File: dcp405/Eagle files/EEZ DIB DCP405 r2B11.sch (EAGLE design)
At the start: 320 parts, among them IC1 LTC3864EMSE#PBF, IC10 MC33272ADR2G, IC11 LTC2050HVCS8#PBF, IC12 74AUP1G74DC.125, IC13 MCP23S17-E/SS, IC14 REF5025AIDR, IC15 TC77-5.0MCTTR, IC16 DAC8552IDGKR, IC17 SN74LVC1G3157DCKR, IC18 ADS1120IPWR, IC19 LM293D, IC2 TPS54060DGQ, IC20 MAX9141ESA, IC3 SI8641BB-B-IS1, IC4 SN74LVC1G139DCUR, IC5 MC78L05, IC6 MC79L05, IC7 SI8641BB-B-IS1, IC8 M24C32-WMN6P, IC9 TL072D, J1 4907, J2 FCR7350R, J3 FCR7350B, K1 G6K-2F-5DC, Q1 SUD19P06-60, Q10 PSMN0R9-25YLC, Q11 PSMN0R9-25YLC, Q12 BSS84P, Q13 BTA26-600, Q14 FMMT493TA, Q15 2N7002, Q16 2N7002, Q17 2N7002, Q18 PSMN013-60YL, Q19 MMBT5551, Q2 MMBT5401, Q20 MMBT5401, Q21 MMBT5551, Q22 MMBT5551, Q23 2N7002, Q3 D45H11FP, Q4 D45H11FP, Q5 FQPF11P06 or FQPF27P06, Q6 BCP56-16.115, Q7 MMBT5401, Q8 NZT605, Q9 BSS205NH6327XTSA1, X1 39-30-1020, X2 77317-104-20LF, X3 691322110005, X4 DS1024-2*10R0

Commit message: DCP405 r2B11
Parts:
- added IC21: SN74LVC1G3157DCKR, EEZ_Lib1:SN74LVC1G3157-DCK
- added Q27: 2N7002, EEZ_Lib1:2N7002
- added R115: 220R, rcl:R-EU_R0805
- added R116: 470R, rcl:R-EU_R0805
- added R118: 22K, rcl:R-EU_R0805
- C55: value 1n -> 4n7
- C62: value N.C. -> 100n; device rcl:C-EUC0805 -> rcl:C-EUC0603
- IC10: value MC33272ADR2G -> TL072D
- R44, R53: value 16K -> 10K
- R62: value 10K -> 47K
- R63: value 220R -> 8K2
- R66: value 750R -> 3K3
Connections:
- new net N$54: IC11A.OUT, R115.2
- new net N$57: IC21.NO, R116.1
- new net N$58: Q27.D, R118.1
- net CC_ACTIVE: now also Q27.G
- net CURR_5A: now also IC21.CTRL
- net GND: now also C62.2, IC21.GND, Q27.S
- net ISENSE-: no longer C62.1
- net I_MON: now also D17.C, IC21.COM, R115.1; no longer C62.2, IC11A.OUT
- net N$81: no longer D17.C
- net N$89: now also R116.2
- net U_SET_OVP: now also R118.2
- net V+: now also C62.1, IC21.VDD
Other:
- note removed: "Parts with red marked values are installed on DCP405 only"
- note removed: "Parts with red marked values are installed on DCP405 only Solder JP2 (0R 0805) on DCP405B"
- note removed: "Parts with red marked values are installed on DCP405 only Solder JP3, JP4 (0R 0805) and use wire jumper instead of F1 and F2 on DCP405B"
- moved on the sheet: C41, C48, C55, C60, C61, C62, D14, D17, IC10A, IC11A, Q10, Q11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

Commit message: DCP405 BOM update
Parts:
- C45: value 1u -> N.C.
- R54: value 4K7 -> 220R
- R55: value N.C. -> 100K
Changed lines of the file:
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@@
 <setting verticaltext="up"/>
 </settings>
-<grid distance="0.1" unitdist="inch" unit="inch" style="lines" multiple="1" display="no" altdistance="0.01" altunitdist="inch" altunit="inch"/>
+<grid distance="0.025" unitdist="inch" unit="inch" style="lines" multiple="4" display="no" altdistance="0.01" altunitdist="inch" altunit="inch"/>
 <layers>
 <layer number="1" name="Top" color="4" fill="1" visible="no" active="no"/>
@@
 <part name="C81" library="rcl" deviceset="C-EU" device="C0603" value="100n"/>
 <part name="C79" library="rcl" deviceset="C-EU" device="C0603" value="100n"/>
-<part name="R55" library="rcl" deviceset="R-EU_" device="R0805" value="N.C."/>
+<part name="R55" library="rcl" deviceset="R-EU_" device="R0805" value="100K"/>
 <part name="P+29" library="supply1" deviceset="+5V" device=""/>
 <part name="R72" library="rcl" deviceset="R-EU_" device="R0805" value="100K"/>
@@
 <part name="R101" library="rcl" deviceset="R-EU_" device="R0805" value="1K"/>
 <part name="R43" library="rcl" deviceset="R-EU_" device="R0805" value="1K"/>
-<part name="R54" library="rcl" deviceset="R-EU_" device="R0805" value="4K7"/>
+<part name="R54" library="rcl" deviceset="R-EU_" device="R0805" value="220R"/>
 <part name="D11" library="EEZ_Lib1" deviceset="DIODE" device="SOD323R" value="BAS316"/>
 <part name="R28" library="rcl" deviceset="R-EU_" device="R0805" value="N.C."/>
@@
 <part name="SUPPLY27" library="supply2" deviceset="-9V" device=""/>
 <part name="SUPPLY44" library="supply2" deviceset="-9V" device=""/>
-<part name="C45" library="rcl" deviceset="C-EU" device="C0805" value="1u"/>
+<part name="C45" library="rcl" deviceset="C-EU" device="C0805" value="N.C."/>
 <part name="SUPPLY6" library="supply2" deviceset="-9V" device=""/>
 <part name="R87" library="rcl" deviceset="R-EU_" device="R0805" value="10K"/>
@@
 <rectangle x1="203.835" y1="91.44" x2="210.82" y2="96.52" layer="97"/>
 <rectangle x1="116.205" y1="130.175" x2="122.555" y2="136.525" layer="97"/>
+<rectangle x1="53.975" y1="76.2" x2="60.96" y2="81.28" layer="97"/>
 </plain>
 <instances>

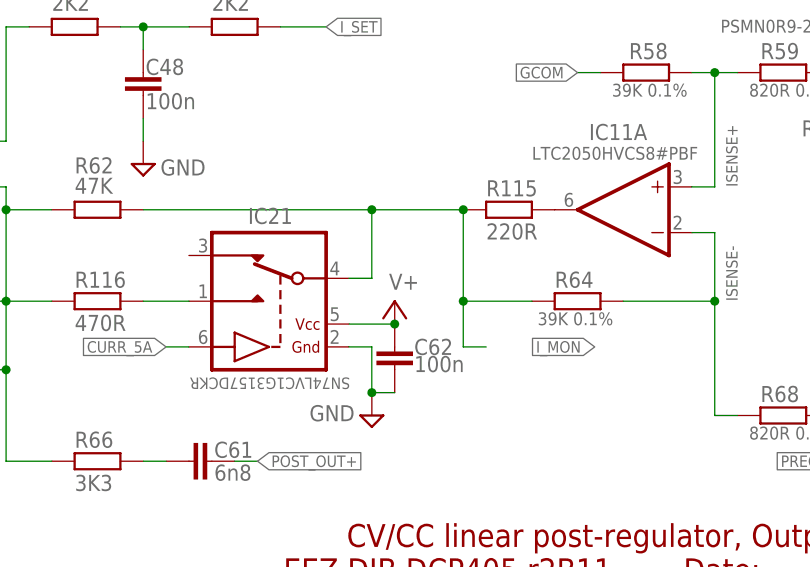
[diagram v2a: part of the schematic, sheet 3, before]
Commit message: DCP405 OVP adjustment
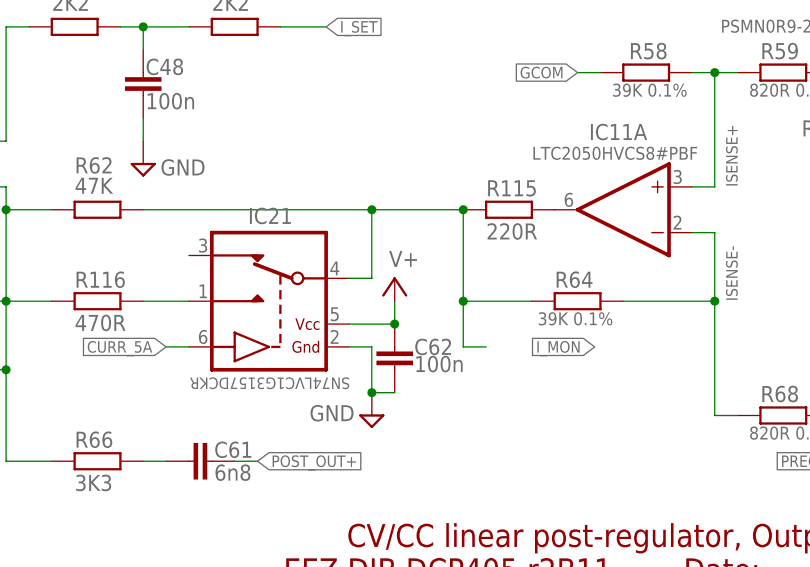
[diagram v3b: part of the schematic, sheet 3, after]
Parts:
- C64: value 1n -> 4n7
- C86: value 1n -> N.C.
- C87: value 33n -> 4n7
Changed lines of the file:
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@@
 <setting verticaltext="up"/>
 </settings>
-<grid distance="0.025" unitdist="inch" unit="inch" style="lines" multiple="4" display="no" altdistance="0.01" altunitdist="inch" altunit="inch"/>
+<grid distance="0.1" unitdist="inch" unit="inch" style="lines" multiple="1" display="no" altdistance="0.01" altunitdist="inch" altunit="inch"/>
 <layers>
 <layer number="1" name="Top" color="4" fill="1" visible="no" active="no"/>
@@
 <part name="R83" library="rcl" deviceset="R-EU_" device="R0805" value="330R"/>
 <part name="R89" library="rcl" deviceset="R-EU_" device="R0805" value="10K"/>
-<part name="C86" library="rcl" deviceset="C-EU" device="C0805" value="1n"/>
+<part name="C86" library="rcl" deviceset="C-EU" device="C0805" value="N.C."/>
 <part name="P+11" library="supply2" deviceset="V+" device=""/>
 <part name="SUPPLY12" library="supply2" deviceset="GND" device=""/>
@@
 <part name="F1" library="EEZ_Lib1" deviceset="ZH32" device="" value="ZH32"/>
 <part name="F2" library="EEZ_Lib1" deviceset="ZH32" device="" value="ZH32"/>
-<part name="C87" library="rcl" deviceset="C-EU" device="C0805" value="33n"/>
+<part name="C87" library="rcl" deviceset="C-EU" device="C0805" value="4n7"/>
 <part name="+3V5" library="supply1" deviceset="+3V3" device=""/>
 <part name="GND2" library="supply1" deviceset="GNDIO" device=""/>
@@
 <part name="C40" library="rcl" deviceset="C-EU" device="C0805" value="N.C."/>
 <part name="JP1" library="EEZ_Lib1" deviceset="JP2-NOCUT" device=""/>
-<part name="C64" library="rcl" deviceset="C-EU" device="C0805" value="1n"/>
+<part name="C64" library="rcl" deviceset="C-EU" device="C0805" value="4n7"/>
 <part name="FM3" library="EEZ_Lib1" deviceset="FIDUCIAL" device="_2"/>
 <part name="D8" library="EEZ_Lib1" deviceset="SCHOTTKY" device="SOD123" value="N.C."/>
@@
 <attribute name="VALUE" x="162.179" y="25.146" size="1.778" layer="96"/>
 </instance>
-<instance part="P+14" gate="1" x="160.02" y="33.02" smashed="yes">
-<attribute name="VALUE" x="159.385" y="34.29" size="1.778" layer="96"/>
+<instance part="P+14" gate="1" x="160.02" y="35.56" smashed="yes">
+<attribute name="VALUE" x="159.385" y="36.83" size="1.778" layer="96"/>
 </instance>
 </instances>
@@
 <pinref part="IC21" gate="G$1" pin="VDD"/>
 <pinref part="C62" gate="G$1" pin="1"/>
-<wire x1="154.94" y1="30.48" x2="160.02" y2="30.48" width="0.1524" layer="91"/>
 <pinref part="P+14" gate="1" pin="V+"/>
+<wire x1="160.02" y1="33.02" x2="160.02" y2="30.48" width="0.1524" layer="91"/>
+<wire x1="154.94" y1="30.48" x2="160.02" y2="30.48" width="0.1524" layer="91"/>
 <junction x="160.02" y="30.48"/>
 </segment>
@@
 <rectangle x1="158.75" y1="135.255" x2="165.1" y2="142.875" layer="97"/>
 <wire x1="259.08" y1="50.8" x2="119.38" y2="50.8" width="0.1524" layer="97" style="shortdash"/>
+<rectangle x1="147.32" y1="129.54" x2="152.4" y2="137.16" layer="97"/>
 </plain>
 <instances>

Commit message: DCP405 fuse rating changed
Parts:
- J2, J3: device EEZ_Lib1:BINDING_POSTCLIFF -> EEZ_connectors:BINDING_POSTCLIFF
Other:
- note added: "5 A quick blow fuse e.g. 179020.5"
- note removed: "Use 6.3A high Breaking capacity fuse e.g. ESKA 522.725"
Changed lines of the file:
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@@
 <layer number="111" name="111" color="7" fill="1" visible="no" active="no"/>
 <layer number="112" name="tSilk" color="7" fill="1" visible="no" active="no"/>
+<layer number="113" name="bTPoint" color="7" fill="1" visible="no" active="no"/>
 <layer number="114" name="EEZ" color="12" fill="1" visible="yes" active="yes"/>
 <layer number="116" name="Patch_BOT" color="7" fill="1" visible="no" active="no"/>
 <layer number="118" name="Rect_Pads" color="7" fill="1" visible="no" active="no"/>
+<layer number="120" name="lotbs" color="7" fill="1" visible="no" active="no"/>
 <layer number="121" name="_tsilk" color="7" fill="1" visible="no" active="no"/>
 <layer number="122" name="_bsilk" color="7" fill="1" visible="no" active="no"/>
@@
 <layer number="132" name="bAdjust" color="7" fill="1" visible="no" active="no"/>
 <layer number="144" name="Drill_legend" color="7" fill="1" visible="no" active="no"/>
+<layer number="148" name="Document_mirrored" color="7" fill="1" visible="no" active="no"/>
 <layer number="150" name="Notes" color="7" fill="1" visible="no" active="no"/>
 <layer number="151" name="HeatSink" color="14" fill="1" visible="no" active="no"/>
@@
 <layer number="154" name="FabDoc2" color="2" fill="1" visible="no" active="no"/>
 <layer number="155" name="FabDoc3" color="7" fill="15" visible="no" active="no"/>
+<layer number="156" name="gesam-Maß" color="1" fill="7" visible="no" active="no"/>
+<layer number="157" name="FaceMchng" color="3" fill="1" visible="no" active="no"/>
+<layer number="158" name="FaceMMeas" color="3" fill="1" visible="no" active="no"/>
+<layer number="159" name="Geh-Bear2" color="1" fill="7" visible="no" active="no"/>
+<layer number="160" name="Topologie" color="9" fill="1" visible="no" active="no"/>
+<layer number="161" name="tomplace2" color="7" fill="1" visible="no" active="no"/>
 <layer number="199" name="Contour" color="7" fill="1" visible="no" active="no"/>
 <layer number="200" name="200bmp" color="1" fill="10" visible="no" active="no"/>
@@
 <layer number="250" name="Descript" color="7" fill="1" visible="no" active="no"/>
 <layer number="251" name="SMDround" color="7" fill="1" visible="no" active="no"/>
+<layer number="252" name="BR-BS" color="7" fill="1" visible="no" active="no"/>
+<layer number="253" name="BR-LS" color="7" fill="1" visible="no" active="no"/>
 <layer number="254" name="OrgLBR" color="13" fill="1" visible="no" active="no"/>
+<layer number="255" name="ZchnBlatt" color="7" fill="1" visible="no" active="no"/>
 </layers>
 <schematic xreflabel="%F%N/%S.%C%R" xrefpart="/%S.%C%R">
@@
 <part name="SUPPLY46" library="supply2" deviceset="GND" device=""/>
 <part name="SUPPLY47" library="supply2" deviceset="GND" device=""/>
-<part name="J3" library="EEZ_Lib1" deviceset="BINDING_POST" device="CLIFF" value="FCR7350B"/>
-<part name="J2" library="EEZ_Lib1" deviceset="BINDING_POST" device="CLIFF" value="FCR7350R"/>
+<part name="J3" library="EEZ_connectors" deviceset="BINDING_POST" device="CLIFF" value="FCR7350B"/>
+<part name="J2" library="EEZ_connectors" deviceset="BINDING_POST" device="CLIFF" value="FCR7350R"/>
 <part name="FRAME6" library="frames" deviceset="DINA4_L" device=""/>
 <part name="R88" library="rcl" deviceset="R-EU_" device="R0805" value="4K7"/>
@@
 <text x="93.98" y="172.72" size="1.778" layer="97">Power output section</text>
 <wire x1="139.7" y1="157.48" x2="261.62" y2="157.48" width="0.1524" layer="97" style="shortdash"/>
-<text x="148.59" y="172.72" size="1.27" layer="103">Use 6.3A high Breaking
-capacity fuse e.g. ESKA 522.725</text>
+<text x="148.59" y="172.72" size="1.27" layer="103">5 A quick blow fuse e.g. 179020.5</text>
 <wire x1="139.7" y1="93.98" x2="139.7" y2="157.48" width="0.1524" layer="97" style="shortdash"/>
 <rectangle x1="182.88" y1="119.38" x2="205.74" y2="137.16" layer="97"/>

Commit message: ULVO levels update for power modules
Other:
- note added: "UVLO off: +26.5 V UVLO on: +27.5 V"
- note removed: "UVLO off: +33 V UVLO on: +38 V"
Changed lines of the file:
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@@
 <wire x1="132.08" y1="35.56" x2="132.08" y2="50.8" width="0.1524" layer="97" style="shortdash"/>
 <wire x1="132.08" y1="50.8" x2="132.08" y2="129.54" width="0.1524" layer="97" style="shortdash"/>
-<text x="34.29" y="161.925" size="1.778" layer="103">UVLO off: +33 V
-UVLO on: +38 V</text>
+<text x="34.29" y="161.925" size="1.778" layer="103">UVLO off: +26.5 V
+UVLO on: +27.5 V</text>
 <text x="110.49" y="128.27" size="1.778" layer="103">+0.8 V</text>
 <text x="111.76" y="177.165" size="1.27" layer="103" rot="MR180">-9 V</text>

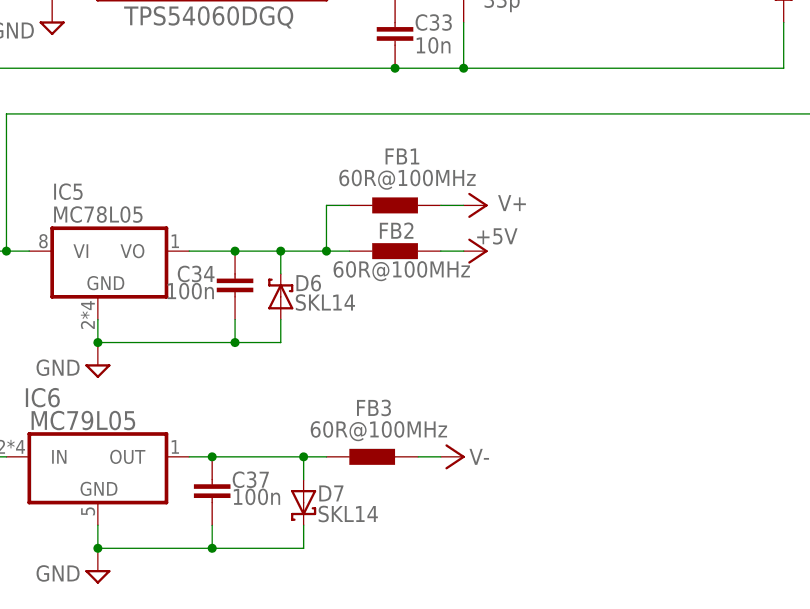
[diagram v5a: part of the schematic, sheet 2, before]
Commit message: FB values updated for DCP405 and DCM220
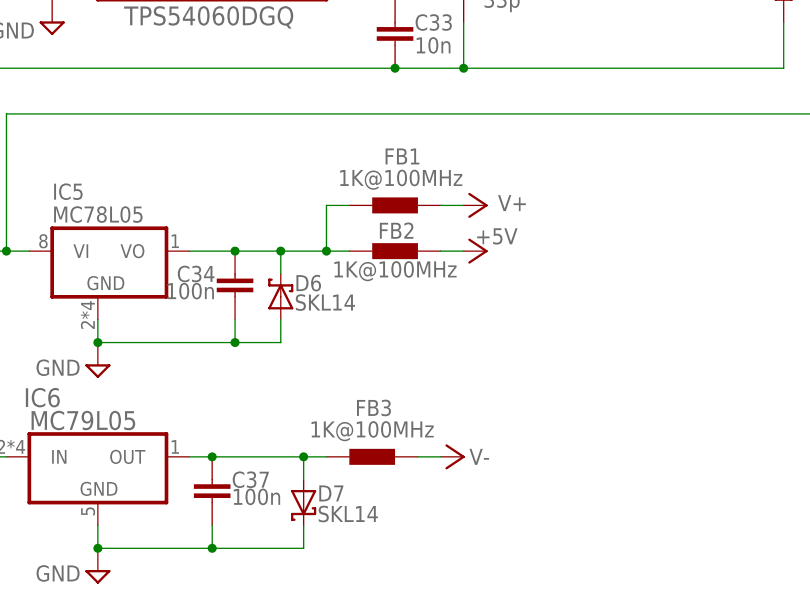
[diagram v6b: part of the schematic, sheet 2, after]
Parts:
- FB1, FB2, FB3: value 60R@100MHz -> 1K@100MHz
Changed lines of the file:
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@@
 <part name="PE5" library="supply1" deviceset="PE" device=""/>
 <part name="SH2" library="EEZ_Lib1" deviceset="SHORT" device="NOHOLE" value="Pgnd to Pout- short"/>
-<part name="FB3" library="EEZ_Lib1" deviceset="FERRITE_BEAD" device="0603" value="60R@100MHz"/>
+<part name="FB3" library="EEZ_Lib1" deviceset="FERRITE_BEAD" device="0603" value="1K@100MHz"/>
 <part name="FRAME9" library="frames" deviceset="DINA4_L" device=""/>
 <part name="R9" library="rcl" deviceset="R-EU_" device="R0805" value="330K"/>
@@
 <part name="P+26" library="supply2" deviceset="V+" device=""/>
 <part name="P+27" library="supply1" deviceset="+5V" device=""/>
-<part name="FB1" library="EEZ_Lib1" deviceset="FERRITE_BEAD" device="0603" value="60R@100MHz"/>
+<part name="FB1" library="EEZ_Lib1" deviceset="FERRITE_BEAD" device="0603" value="1K@100MHz"/>
 <part name="R2" library="rcl" deviceset="R-EU_" device="R0805" value="10K"/>
 <part name="C19" library="rcl" deviceset="C-EU" device="C0805" value="470p"/>
-<part name="FB2" library="EEZ_Lib1" deviceset="FERRITE_BEAD" device="0603" value="60R@100MHz"/>
+<part name="FB2" library="EEZ_Lib1" deviceset="FERRITE_BEAD" device="0603" value="1K@100MHz"/>
 <part name="C4" library="rcl" deviceset="C-EU" device="C1206" value="10n/200V"/>
 <part name="C3" library="rcl" deviceset="C-EU" device="C1206" value="10n/200V"/>
